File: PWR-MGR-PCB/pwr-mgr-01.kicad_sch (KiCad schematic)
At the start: 23 parts, among them J3 USB_C_Receptacle_USB2.0_14P, J4 Battery_1x2, U2 BQ24074RGT, U5 USBLC6-2SC6, U6 TPS631011YBGR

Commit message: Change USB-C to 6 pin
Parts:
- J3: footprint Connector_USB:USB_C_Receptacle_GCT_USB4105-xx-A_16P_TopMnt_Horizontal -> Connector_USB:USB_C_Receptacle_GCT_USB4135-GF-A_6P_TopMnt_Horizontal
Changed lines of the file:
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@@
 			)
 		)
-		(property "Footprint" "Connector_USB:USB_C_Receptacle_GCT_USB4105-xx-A_16P_TopMnt_Horizontal"
+		(property "Footprint" "Connector_USB:USB_C_Receptacle_GCT_USB4135-GF-A_6P_TopMnt_Horizontal"
 			(at 57.15 81.28 0)
 			(effects

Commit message: Switch back to 16 pin
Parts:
- J3: footprint Connector_USB:USB_C_Receptacle_GCT_USB4135-GF-A_6P_TopMnt_Horizontal -> Connector_USB:USB_C_Receptacle_GCT_USB4105-xx-A_16P_TopMnt_Horizontal
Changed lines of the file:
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@@
 			)
 		)
-		(property "Footprint" "Connector_USB:USB_C_Receptacle_GCT_USB4135-GF-A_6P_TopMnt_Horizontal"
+		(property "Footprint" "Connector_USB:USB_C_Receptacle_GCT_USB4105-xx-A_16P_TopMnt_Horizontal"
 			(at 57.15 81.28 0)
 			(effects

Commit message: Improve USB routing
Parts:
- added C3: 100 uF, Capacitor_SMD:C_0805_2012Metric, symbol Device:C
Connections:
- net GND: now also C3.2
- net USB_CONN_D+: now also U5.3 (I/O2); no longer U5.1 (I/O1)
- net USB_CONN_D-: now also U5.1 (I/O1); no longer U5.3 (I/O2)
- net USB_D+: now also U5.4 (I/O2); no longer U5.6 (I/O1)
- net USB_D-: now also U5.6 (I/O1); no longer U5.4 (I/O2)
- net VBUS 5V: now also C3.1
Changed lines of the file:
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@@
 	)
 	(junction
+		(at 129.54 66.04)
+		(diameter 0)
+		(color 0 0 0 0)
+	)
+	(junction
 		(at 71.12 85.09)
 		(diameter 0)
@@
 	(wire
 		(pts
-			(xy 115.57 76.2) (xy 116.84 76.2)
+			(xy 114.3 76.2) (xy 116.84 76.2)
 		)
 		(stroke
@@
 	(wire
 		(pts
+			(xy 151.13 66.04) (xy 151.13 67.31)
+		)
+		(stroke
+			(width 0)
+			(type default)
+		)
+	)
+	(wire
+		(pts
 			(xy 71.12 80.01) (xy 71.12 81.28)
 		)
@@
 	(wire
 		(pts
+			(xy 133.35 66.04) (xy 129.54 66.04)
+		)
+		(stroke
+			(width 0)
+			(type default)
+		)
+	)
+	(wire
+		(pts
 			(xy 52.07 130.81) (xy 52.07 152.4)
 		)
@@
 	(wire
 		(pts
+			(xy 129.54 66.04) (xy 129.54 62.23)
+		)
+		(stroke
+			(width 0)
+			(type default)
+		)
+	)
+	(wire
+		(pts
 			(xy 71.12 80.01) (xy 77.47 80.01)
 		)
@@
 	(wire
 		(pts
-			(xy 115.57 86.36) (xy 116.84 86.36)
+			(xy 114.3 86.36) (xy 116.84 86.36)
+		)
+		(stroke
+			(width 0)
+			(type default)
+		)
+	)
+	(wire
+		(pts
+			(xy 140.97 66.04) (xy 151.13 66.04)
 		)
 		(stroke
@@
 	(wire
 		(pts
-			(xy 129.54 68.58) (xy 129.54 67.31)
+			(xy 129.54 68.58) (xy 129.54 66.04)
 		)
 		(stroke
@@
 		)
 	)
-	(label "USB_CONN_D-"
-		(at 115.57 86.36 180)
-		(effects
-			(font
-				(size 1.27 1.27)
-			)
-			(justify right bottom)
-		)
-	)
 	(label "V_BATT"
 		(at 106.68 147.32 0)
@@
 		)
 	)
-	(label "USB_CONN_D+"
-		(at 115.57 76.2 180)
+	(label "VCC_BMS"
+		(at 101.6 139.7 0)
 		(effects
 			(font
 				(size 1.27 1.27)
 			)
-			(justify right bottom)
+			(justify left bottom)
 		)
 	)
-	(label "VCC_BMS"
-		(at 101.6 139.7 0)
+	(label "USB_CONN_D-"
+		(at 114.3 76.2 180)
 		(effects
 			(font
 				(size 1.27 1.27)
 			)
-			(justify left bottom)
+			(justify right bottom)
 		)
 	)
@@
 		)
 	)
+	(label "USB_CONN_D+"
+		(at 114.3 86.36 180)
+		(effects
+			(font
+				(size 1.27 1.27)
+			)
+			(justify right bottom)
+		)
+	)
 	(label "+3.3V"
 		(at 259.08 78.74 0)
@@
 		)
 	)
-	(hierarchical_label "USB_D+"
+	(hierarchical_label "3.3V"
 		(shape output)
-		(at 147.32 76.2 0)
+		(at 259.08 73.66 0)
 		(effects
 			(font
@@
 		)
 	)
-	(hierarchical_label "3.3V"
+	(hierarchical_label "USB_D-"
 		(shape output)
-		(at 259.08 73.66 0)
+		(at 147.32 76.2 0)
 		(effects
 			(font
@@
 		)
 	)
-	(hierarchical_label "USB_D-"
+	(hierarchical_label "USB_D+"
 		(shape output)
 		(at 147.32 86.36 0)
@@
 	)
 	(symbol
+		(lib_id "power:GND")
+		(at 151.13 67.31 0)
+		(unit 1)
+		(exclude_from_sim no)
+		(in_bom yes)
+		(on_board yes)
+		(dnp no)
+		(fields_autoplaced yes)
+		(property "Reference" "#PWR01"
+			(at 151.13 73.66 0)
+			(effects
+				(font
+					(size 1.27 1.27)
+				)
+				(hide yes)
+			)
+		)
+		(property "Value" "GND"
+			(at 151.13 72.39 0)
+			(effects
+				(font
+					(size 1.27 1.27)
+				)
+			)
+		)
+		(property "Footprint" ""
+			(at 151.13 67.31 0)
+			(effects
+				(font
+					(size 1.27 1.27)
+				)
+				(hide yes)
+			)
+		)
+		(property "Datasheet" ""
+			(at 151.13 67.31 0)
+			(effects
+				(font
+					(size 1.27 1.27)
+				)
+				(hide yes)
+			)
+		)
+		(property "Description" "Power symbol creates a global label with name \"GND\" , ground"
+			(at 151.13 67.31 0)
+			(effects
+				(font
+					(size 1.27 1.27)
+				)
+				(hide yes)
+			)
+		)
+		(pin "1"
+		)
+		(instances
+			(project "PWR-MGR-PCB"
+				(path "/16b2e4e2-6399-42b6-a8e6-a11780888710/aa25d2a4-7317-40e7-833e-e05b81834ee4"
+					(reference "#PWR01")
+					(unit 1)
+				)
+			)
+		)
+	)
+	(symbol
 		(lib_id "Connector:Conn_01x02_Pin")
 		(at 120.65 158.75 180)
@@
 	(symbol
 		(lib_id "power:VBUS")
-		(at 129.54 67.31 0)
+		(at 129.54 62.23 0)
 		(unit 1)
 		(exclude_from_sim no)
@@
 		(fields_autoplaced yes)
 		(property "Reference" "#PWR032"
-			(at 129.54 71.12 0)
+			(at 129.54 66.04 0)
 			(effects
 				(font
@@
 		)
 		(property "Value" "VBUS 5V"
-			(at 129.54 62.23 0)
+			(at 129.54 57.15 0)
 			(effects
 				(font
@@
 		)
 		(property "Footprint" ""
-			(at 129.54 67.31 0)
+			(at 129.54 62.23 0)
 			(effects
 				(font
@@
 		)
 		(property "Datasheet" ""
-			(at 129.54 67.31 0)
+			(at 129.54 62.23 0)
 			(effects
 				(font
@@
 		)
 		(property "Description" "Power symbol creates a global label with name \"VBUS\""
-			(at 129.54 67.31 0)
+			(at 129.54 62.23 0)
 			(effects
 				(font
@@
 		(dnp no)
 		(property "Reference" "U5"
-			(at 128.27 54.61 0)
+			(at 128.27 52.832 0)
 			(effects
 				(font
@@
 		)
 		(property "Value" "USBLC6-2SC6"
-			(at 122.936 56.896 0)
+			(at 122.936 54.864 0)
 			(effects
 				(font
@@
 					(unit 1)
 				)
+			)
+		)
+	)
+	(symbol
+		(lib_id "Device:C")
+		(at 137.16 66.04 90)
+		(unit 1)
+		(exclude_from_sim no)
+		(in_bom yes)
+		(on_board yes)
+		(dnp no)
+		(property "Reference" "C3"
+			(at 138.176 60.706 90)
+			(effects
+				(font
+					(size 1.27 1.27)
+				)
+				(justify left)
+			)
+		)
+		(property "Value" "100 uF"
+			(at 141.986 62.484 90)
+			(effects
+				(font
+					(size 1.27 1.27)
+				)
+				(justify left)
+			)
+		)
+		(property "Footprint" "Capacitor_SMD:C_0805_2012Metric"
+			(at 140.97 65.0748 0)
+			(effects
+				(font
+					(size 1.27 1.27)
+				)
+				(hide yes)
+			)
+		)
+		(property "Datasheet" "~"
+			(at 137.16 66.04 0)
+			(effects
+				(font
+					(size 1.27 1.27)
+				)
+				(hide yes)
+			)
+		)
+		(property "Description" "Unpolarized capacitor"
+			(at 137.16 66.04 0)
+			(effects
+				(font
+					(size 1.27 1.27)
+				)
+				(hide yes)
+			)
+		)
+		(pin "2"
+		)
+		(pin "1"
+		)
+		(instances
+			(project "PWR-MGR-PCB"
+				(path "/16b2e4e2-6399-42b6-a8e6-a11780888710/aa25d2a4-7317-40e7-833e-e05b81834ee4"
+					(reference "C3")
+					(unit 1)
+				)

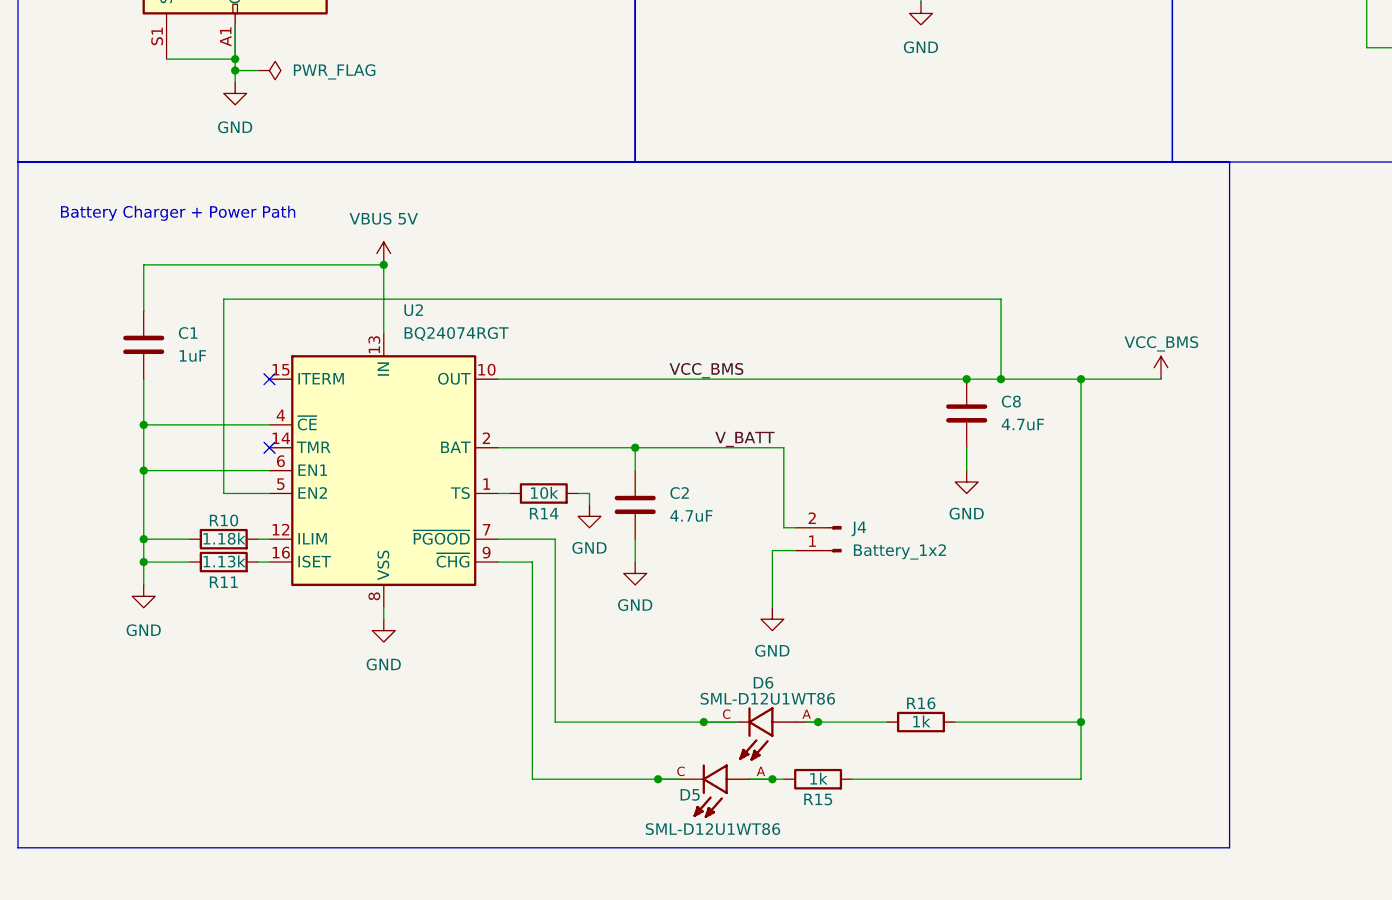
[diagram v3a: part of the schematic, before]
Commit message: Add BQ24075
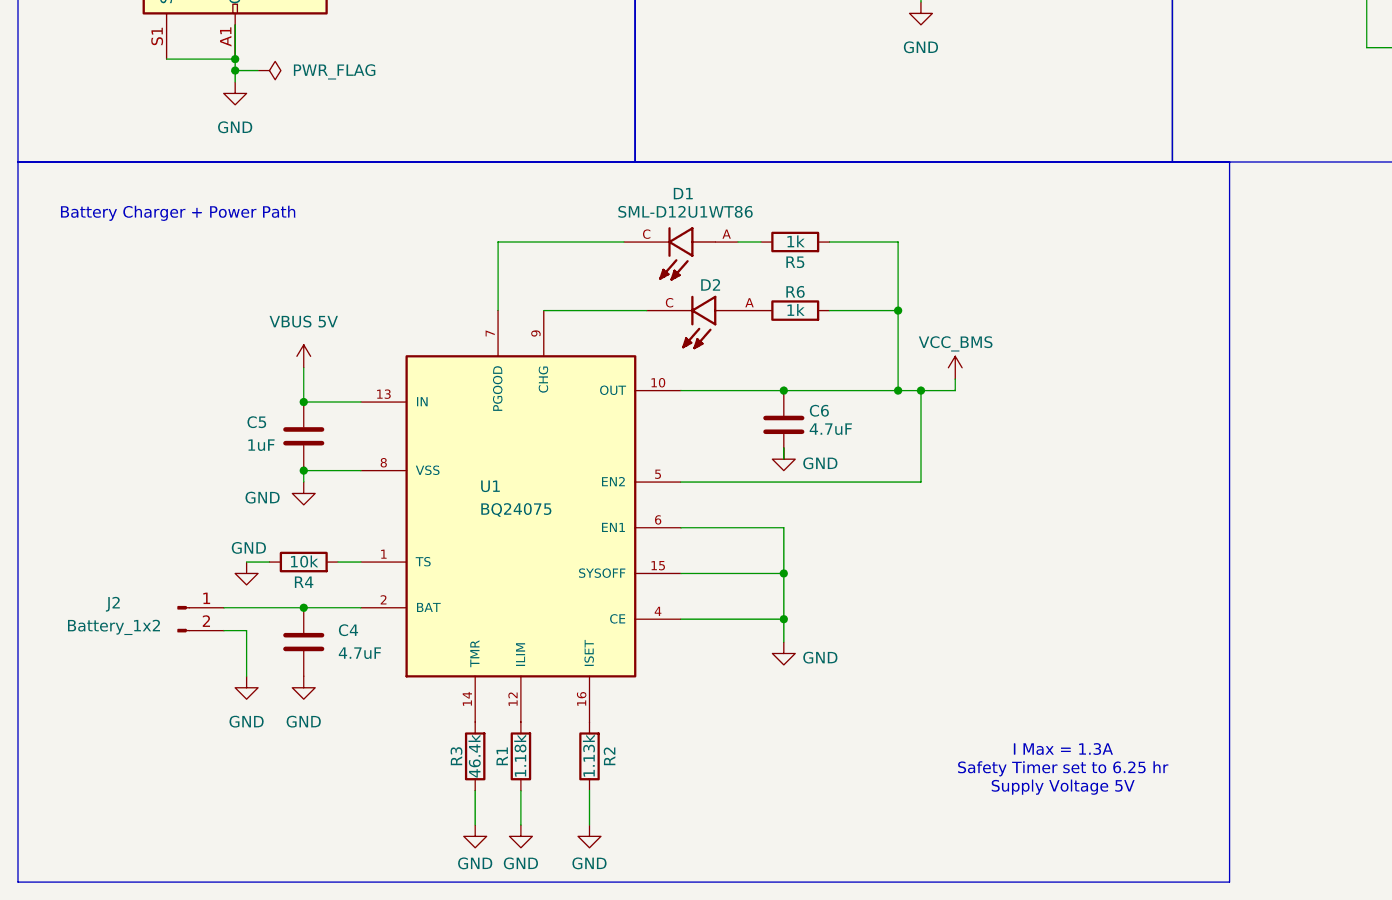
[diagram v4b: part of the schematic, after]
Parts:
- removed C1: 1uF, Capacitor_SMD:C_0805_2012Metric, symbol Device:C
- removed C2, C8: 4.7uF, Capacitor_SMD:C_0805_2012Metric, symbol Device:C
- removed D5, D6: SML-D12U1WT86, LED - SML_D12U1WT86:LED_SML-D12U1WT86, symbol SML-D12U1WT86:SML-D12U1WT86
- removed J4: Battery_1x2, Connector_JST:JST_PH_B2B-PH-K_1x02_P2.00mm_Vertical, symbol Connector:Conn_01x02_Pin
- removed R10: 1.18k, Resistor_SMD:R_0805_2012Metric, symbol Device:R
- removed R11: 1.13k, Resistor_SMD:R_0805_2012Metric, symbol Device:R
- removed R14: 10k, Resistor_SMD:R_0805_2012Metric, symbol Device:R
- removed R15, R16: 1k, Resistor_SMD:R_0805_2012Metric, symbol Device:R
- removed U2: BQ24074RGT, BQ24074RGTR:QFN50P300X300X100-17N, symbol Battery_Management:BQ24074RGT
- added C4, C6: 4.7uF, Capacitor_SMD:C_0805_2012Metric, symbol Device:C
- added C5: 1uF, Capacitor_SMD:C_0805_2012Metric, symbol Device:C
- added D1, D2: SML-D12U1WT86, LED - SML_D12U1WT86:LED_SML-D12U1WT86, symbol SML-D12U1WT86:SML-D12U1WT86
- added J2: Battery_1x2, Connector_JST:JST_PH_B2B-PH-K_1x02_P2.00mm_Vertical, symbol Connector:Conn_01x02_Pin
- added R1: 1.18k, Resistor_SMD:R_0805_2012Metric, symbol Device:R
- added R2: 1.13k, Resistor_SMD:R_0805_2012Metric, symbol Device:R
- added R3: 46.4k, Resistor_SMD:R_0805_2012Metric, symbol Device:R
- added R4: 10k, Resistor_SMD:R_0805_2012Metric, symbol Device:R
- added R5, R6: 1k, Resistor_SMD:R_0805_2012Metric, symbol Device:R
- added U1: BQ24075, BQ24075:QFN16, symbol BQ24075:BQ24075
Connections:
- net GND: now also C4.2, C5.2, C6.2, J2.2 (Pin_2), R1.1, R2.1, R3.1, R4.1, U1.15 (SYSOFF), U1.4 (CE), U1.6 (EN1), U1.8 (VSS), U1.TH (VSS)
- net VBUS 5V: now also C5.1, U1.13 (IN)
- net VCC_BMS: now also C6.1, R5.2, R6.2, U1.10 (OUT), U1.5 (EN2)
- new net: D1.A, R5.1
- new net: R3.2, U1.14 (TMR)
- new net: D1.C, U1.7 (PGOOD)
- new net: R4.2, U1.1 (TS)
- new net: R1.2, U1.12 (ILIM)
- new net: R2.2, U1.16 (ISET)
- new net: C4.1, J2.1 (Pin_1), U1.2 (BAT), U1.3 (BAT)
- new net: D2.C, U1.9 (CHG)
- new net: D2.A, R6.1
- no-connect marks 2 -> 0
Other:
- note added: "I Max = 1.3A Safety Timer set to 6.25 hr Supply Voltage 5V"

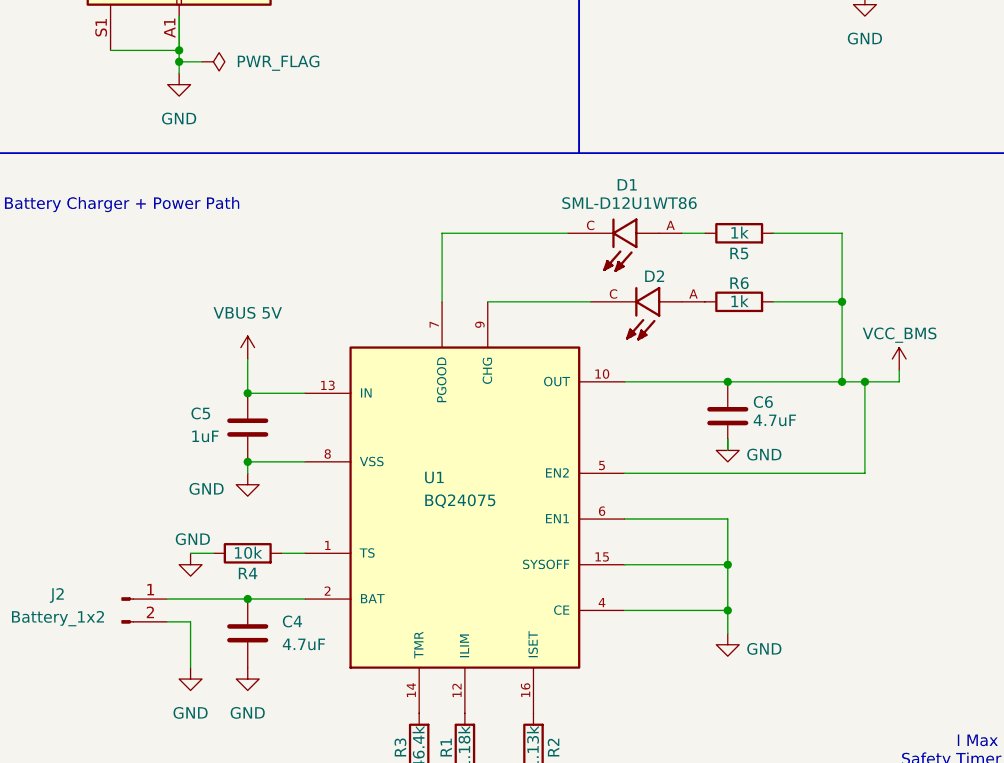
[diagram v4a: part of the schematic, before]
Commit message: Route BQ24075
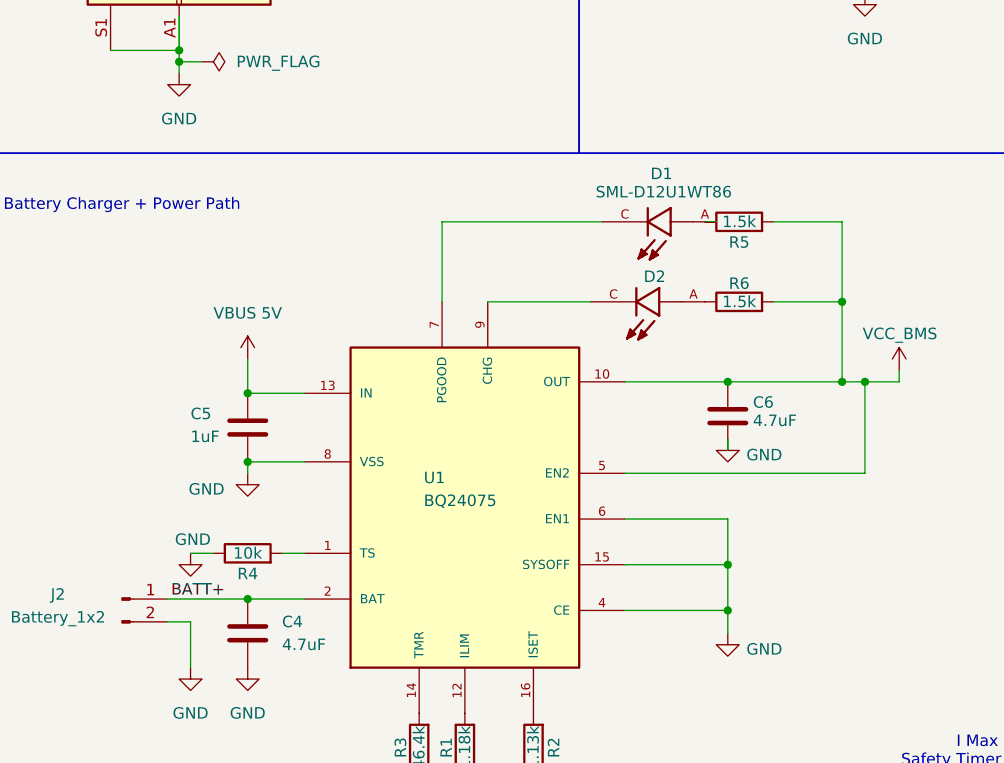
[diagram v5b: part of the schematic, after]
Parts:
- R5, R6: value 1k -> 1.5k
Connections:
- net BATT+: now reaches C4.1, J2.1 (Pin_1), U1.2 (BAT), U1.3 (BAT)
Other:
- moved on the sheet: D1, R5
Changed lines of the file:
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@@
 	(wire
 		(pts
-			(xy 127 124.46) (xy 127 132.08)
+			(xy 127 123.19) (xy 127 132.08)
 		)
 		(stroke
@@
 	(wire
 		(pts
-			(xy 96.52 124.46) (xy 82.55 124.46)
+			(xy 100.33 123.19) (xy 82.55 123.19)
 		)
 		(stroke
@@
 	(wire
 		(pts
-			(xy 82.55 124.46) (xy 82.55 132.08)
+			(xy 82.55 123.19) (xy 82.55 132.08)
 		)
 		(stroke
@@
 	(wire
 		(pts
-			(xy 119.38 124.46) (xy 127 124.46)
+			(xy 119.38 123.19) (xy 127 123.19)
 		)
 		(stroke
@@
 	(wire
 		(pts
-			(xy 109.22 124.46) (xy 111.76 124.46)
+			(xy 113.03 123.19) (xy 111.76 123.19)
 		)
 		(stroke
@@
 			)
 			(justify left bottom)
+		)
+	)
+	(label "BATT+"
+		(at 58.42 165.1 180)
+		(effects
+			(font
+				(size 1.27 1.27)
+			)
+			(justify right bottom)
 		)
 	)
@@
 	(symbol
 		(lib_id "Device:R")
-		(at 115.57 124.46 90)
+		(at 115.57 123.19 90)
 		(unit 1)
 		(exclude_from_sim no)
@@
 		(dnp no)
 		(property "Reference" "R5"
-			(at 115.57 126.746 90)
-			(effects
-				(font
-					(size 1.27 1.27)
-				)
-			)
-		)
-		(property "Value" "1k"
-			(at 115.57 124.46 90)
+			(at 115.57 125.476 90)
+			(effects
+				(font
+					(size 1.27 1.27)
+				)
+			)
+		)
+		(property "Value" "1.5k"
+			(at 115.57 123.19 90)
 			(effects
 				(font
@@
 		)
 		(property "Footprint" "Resistor_SMD:R_0805_2012Metric"
-			(at 115.57 126.238 90)
+			(at 115.57 124.968 90)
 			(effects
 				(font
@@
 		)
 		(property "Datasheet" "~"
-			(at 115.57 124.46 0)
+			(at 115.57 123.19 0)
 			(effects
 				(font
@@
 		)
 		(property "Description" "Resistor"
-			(at 115.57 124.46 0)
+			(at 115.57 123.19 0)
 			(effects
 				(font
@@
 	(symbol
 		(lib_id "SML-D12U1WT86:SML-D12U1WT86")
-		(at 101.6 124.46 180)
+		(at 105.41 123.19 180)
 		(unit 1)
 		(exclude_from_sim no)
@@
 		(dnp no)
 		(property "Reference" "D1"
-			(at 103.124 119.126 0)
+			(at 106.934 117.856 0)
 			(effects
 				(font
@@
 		)
 		(property "Value" "SML-D12U1WT86"
-			(at 103.378 121.158 0)
+			(at 107.188 119.888 0)
 			(effects
 				(font
@@
 		)
 		(property "Footprint" "LED - SML_D12U1WT86:LED_SML-D12U1WT86"
-			(at 101.6 124.46 0)
+			(at 105.41 123.19 0)
 			(effects
 				(font
@@
 		)
 		(property "Datasheet" ""
-			(at 101.6 124.46 0)
+			(at 105.41 123.19 0)
 			(effects
 				(font
@@
 		)
 		(property "Description" ""
-			(at 101.6 124.46 0)
+			(at 105.41 123.19 0)
 			(effects
 				(font
@@
 		)
 		(property "PARTREV" "007"
-			(at 101.6 124.46 0)
+			(at 105.41 123.19 0)
 			(effects
 				(font
@@
 		)
 		(property "MANUFACTURER" "ROHM Semiconductor"
-			(at 101.6 124.46 0)
+			(at 105.41 123.19 0)
 			(effects
 				(font
@@
 		)
 		(property "MAXIMUM_PACKAGE_HEIGHT" "0.65 mm"
-			(at 101.6 124.46 0)
+			(at 105.41 123.19 0)
 			(effects
 				(font
@@
 		)
 		(property "STANDARD" "Manufacturer Recommendation"
-			(at 101.6 124.46 0)
+			(at 105.41 123.19 0)
 			(effects
 				(font
@@
 			)
 		)
-		(property "Value" "1k"
+		(property "Value" "1.5k"
 			(at 115.57 132.08 90)
 			(effects

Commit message: Solve all ERC issues
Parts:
- U6: value TPS631011YBGR -> TPS631011YBGR-Pin_Corrected; footprint TPS631011 - Buck Boost Converter:DSBGA8_YBG_TEX -> DSBGA8_YBG_TEX; symbol TPS631011:TPS631011YBGR -> TPS631011:TPS631011YBGR-Pin_Corrected
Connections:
- no-connect marks 0 -> 1
